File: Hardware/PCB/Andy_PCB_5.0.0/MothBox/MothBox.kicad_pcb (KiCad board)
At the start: 2 copper layers, 237.2 x 140.5 mm, 189 parts, among them J1 Screw_Terminal_01x02, J2 TYPE-C-31-M-17, J4 GPS Header, J5 Conn_01x05_Pin, J7 DC Power Jack, Q1 IRF9540N, Q10 BC817, Q11 BC817, Q2 TJ10S04M3L,LXHQ, Q3 BC817, Q4 TJ10S04M3L,LXHQ, Q5 TJ10S04M3L,LXHQ, Q6 BC817, Q7 BC817, Q8 BC817, Q9 BC817, SW1 SW_Push, SW2 Days, SW3 Power, SW4 Sequence+Toggle, SW5 Hours, SW6 Hours, U1 XL4015, U10 IRF9335TRPBF, U11 IRF9335TRPBF, U12 CD74HC4067M96E4, U13 CD74HC4067M96E4, U2 9V-36V to 12V 5A 60W, U3 RASPBERRY_PI_5, U4 RASPBERRY_PI_4B_4GB, U5 STM32L031K6Tx, U6 TLV75733PDBVR, U8 IRF9335TRPBF, U9 IRF9335TRPBF, Y1 32.768kHz

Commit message: made better camera
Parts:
- REF**: moved to F.Cu
- moved REF** 7.28 mm to (149.5, 131.8)
- moved REF** 3.00 mm to (125.5, 195.8)
- moved REF** 2.00 mm to (154.5, 195.8)
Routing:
- net Net-(Q5-G): track 8.96 -> 0.00 mm
- net /Photo LED's/+12V_R_LED: track 467.2 -> 476.2 mm
- net Net-(Q4-G): track 8.19 -> 0.00 mm
- net /Photo LED's/+12V_L_LED: track 483.1 -> 491.3 mm
- net Net-(Q2-G): track 7.03 -> 0.00 mm
- net /Power/VBUS: track 0.00 -> 7.03 mm
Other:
- outline, holes or cut-outs redrawn

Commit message: before overhaul from Troublemaker meeting
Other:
- board text added: "V5.0.0"

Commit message: added female inverted header
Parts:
- removed C10, C11: 12pF, Capacitor_SMD:C_0805_2012Metric
- removed C13, C14, C15, C18, C9: 0.1uF, Capacitor_SMD:C_0805_2012Metric
- removed C6, C7: 1uF, Capacitor_SMD:C_0805_2012Metric
- removed C8: 100nF, Capacitor_SMD:C_0805_2012Metric
- removed D10, D11, D12, D13, D14, D15, D16, D17, D18, D19, D2, D20, D3, D4, D5, D6, D7, D8, D9: LED, LED_SMD:LED_Everlight-SMD3528_3.5x2.8mm_67-21ST
- removed D21, D22, D23, D24, D25, D26, D27, D28: LED, LED_SMD:LED_0805_2012Metric
- removed D29, D36: ESD12VD3B-TP, Diode_SMD:D_SOD-323
- removed E1: BZT52Bxx, Diode_SMD:D_SOD-123F
- removed E2: SMBJ36A, Diode_SMD:D_SMB
- removed E4: SK54C, SK54C:DIO_SK54C
- removed F1: 7A Fuse, Fuse:Fuseholder_Clip-5x20mm_Eaton_1A5601-01_Inline_P20.80x6.76mm_D1.70mm_Horizontal
- removed J1: Screw_Terminal_01x02, TerminalBlock_RND:TerminalBlock_RND_205-00023_1x02_P10.00mm_Horizontal
- removed J2: TYPE-C-31-M-17, TYPE-C-31-M-17:TYPEC31M17
- removed J4: GPS Header, GPS_MAX10:Untitled
- removed J5: Conn_01x05_Pin, Connector_PinHeader_2.54mm:PinHeader_1x05_P2.54mm_Vertical
- removed J7: DC Power Jack, Connector_BarrelJack:BarrelJack_GCT_DCJ200-10-A_Horizontal
- removed Q1: IRF9540N, Package_TO_SOT_THT:TO-220-3_Vertical
- removed Q2: TJ10S04M3L,LXHQ, Package_TO_SOT_SMD:TO-252-2
- removed Q3: BC817, Package_TO_SOT_SMD:SOT-23
- removed R1: 10k, Resistor_SMD:R_0805_2012Metric
- removed R61, R62, R63, R64, R65, R67, R68, R70, R71, R72, R73, R74: 170R, Resistor_SMD:R_2512_6332Metric
- removed R83, R84, R85, R86: DNP, Resistor_SMD:R_0805_2012Metric
- removed REF** (x10): MountingHole_6.4mm_M6_Pad_wSTEP, AQLibrary:MountingHole_6.4mm_M6_Pad_wSTEP
- removed REF**: Arducam Owlsight, Attractor:Arducam Owlsight
- removed SW1: SW_Push, TS-1187A-B-A-B:SW_TS-1187A-B-A-B
- removed SW2: Days, DS04-254-2-07BK-SMT:SW_DS04-254-2-07BK-SMT
- removed SW3: Power, DS04-254-2-03BK-SMT1:SW_DS04-254-2-03BK-SMT
- removed SW4: Sequence+Toggle, DS04-254-2-04BK-SMT:SW_DS04-254-2-04BK-SMT
- removed SW5: Hours, DS04-254-2-07BK-SMT:SW_DS04-254-2-07BK-SMT
- removed SW6: Hours, DS04-254-2-06BK-SMT:SW_DS04-254-2-06BK-SMT
- removed Y1: 32.768kHz, Crystal:Crystal_SMD_3215-2Pin_3.2x1.5mm
- added B1: ~, AQLibrary:Talentcell, B.Cu at (117.2, 172.8)
- added D32: ESD12VD3B-TP, Diode_SMD:D_SOD-323, F.Cu at (22.1, 26.1)
- added F2: Polyfuse, Fuse:Fuse_Bourns_MF-RG1000, F.Cu at (203.7, 287.4)
- added H1: MountingHole_1/4inbolt, MountingHole:MountingHole_6.4mm_M6_Pad, F.Cu at (43.5, 70.8)
- added H2: MountingHole_1/4inbolt, MountingHole:MountingHole_6.4mm_M6_Pad, F.Cu at (155.5, 70.8)
- added H3: MountingHole_1/4inbolt, MountingHole:MountingHole_6.4mm_M6_Pad, F.Cu at (38.5, 77.8)
- added H4: MountingHole_1/4inbolt, MountingHole:MountingHole_6.4mm_M6_Pad, F.Cu at (163.5, 53.8)
- added H5: MountingHole_1/4inbolt, MountingHole:MountingHole_6.4mm_M6_Pad, F.Cu at (255.5, 192.8)
- added H6: MountingHole_1/4inbolt, MountingHole:MountingHole_6.4mm_M6_Pad, F.Cu at (41.5, 187.8)
- added H7: MountingHole_1/4inbolt, MountingHole:MountingHole_6.4mm_M6_Pad, F.Cu at (257.5, 178.8)
- added H8: MountingHole_1/4inbolt, MountingHole:MountingHole_6.4mm_M6_Pad, F.Cu at (42.5, 138.8)
- added LED1: XL-2835UWC-02, easyeda2kicad:LED-SMD_L3.5-W2.8-RD_1.25T-2PWT, F.Cu at (87.5, 223.8)
- added LED10: XL-2835UWC-02, easyeda2kicad:LED-SMD_L3.5-W2.8-RD_1.25T-2PWT, F.Cu at (94.1, 228.5)
- added LED11: XL-2835UWC-02, easyeda2kicad:LED-SMD_L3.5-W2.8-RD_1.25T-2PWT, F.Cu at (94.1, 232.5)
- added LED12: XL-2835UWC-02, easyeda2kicad:LED-SMD_L3.5-W2.8-RD_1.25T-2PWT, F.Cu at (94.1, 236.6)
- added LED13: XL-2835UWC-02, easyeda2kicad:LED-SMD_L3.5-W2.8-RD_1.25T-2PWT, F.Cu at (94.1, 240.6)
- added LED14: XL-2835UWC-02, easyeda2kicad:LED-SMD_L3.5-W2.8-RD_1.25T-2PWT, F.Cu at (94.1, 244.7)
- added LED15: XL-2835UWC-02, easyeda2kicad:LED-SMD_L3.5-W2.8-RD_1.25T-2PWT, F.Cu at (94.1, 248.7)
- added LED16: XL-2835UWC-02, easyeda2kicad:LED-SMD_L3.5-W2.8-RD_1.25T-2PWT, F.Cu at (94.1, 252.8)
- added LED17: XL-2835UWC-02, easyeda2kicad:LED-SMD_L3.5-W2.8-RD_1.25T-2PWT, F.Cu at (99.7, 224.4)
- added LED18: XL-2835UWC-02, easyeda2kicad:LED-SMD_L3.5-W2.8-RD_1.25T-2PWT, F.Cu at (99.7, 228.5)
- added LED19: XL-2835UWC-02, easyeda2kicad:LED-SMD_L3.5-W2.8-RD_1.25T-2PWT, F.Cu at (99.7, 232.5)
- added LED2: XL-2835UWC-02, easyeda2kicad:LED-SMD_L3.5-W2.8-RD_1.25T-2PWT, F.Cu at (88.5, 228.5)
- added LED20: XL-2835UWC-02, easyeda2kicad:LED-SMD_L3.5-W2.8-RD_1.25T-2PWT, F.Cu at (99.7, 236.6)
- added LED21: XL-2835UWC-02, easyeda2kicad:LED-SMD_L3.5-W2.8-RD_1.25T-2PWT, F.Cu at (99.7, 240.6)
- added LED22: XL-2835UWC-02, easyeda2kicad:LED-SMD_L3.5-W2.8-RD_1.25T-2PWT, F.Cu at (99.7, 244.7)
- added LED23: XL-2835UWC-02, easyeda2kicad:LED-SMD_L3.5-W2.8-RD_1.25T-2PWT, F.Cu at (99.7, 248.7)
- added LED24: XL-2835UWC-02, easyeda2kicad:LED-SMD_L3.5-W2.8-RD_1.25T-2PWT, F.Cu at (99.7, 252.8)
- added LED25: XL-2835UWC-02, easyeda2kicad:LED-SMD_L3.5-W2.8-RD_1.25T-2PWT, F.Cu at (105.3, 224.4)
- added LED26: XL-2835UWC-02, easyeda2kicad:LED-SMD_L3.5-W2.8-RD_1.25T-2PWT, F.Cu at (105.3, 228.5)
- added LED27: XL-2835UWC-02, easyeda2kicad:LED-SMD_L3.5-W2.8-RD_1.25T-2PWT, F.Cu at (105.3, 232.5)
- added LED28: XL-2835UWC-02, easyeda2kicad:LED-SMD_L3.5-W2.8-RD_1.25T-2PWT, F.Cu at (105.3, 236.6)
- added LED29: XL-2835UWC-02, easyeda2kicad:LED-SMD_L3.5-W2.8-RD_1.25T-2PWT, F.Cu at (105.3, 240.6)
- added LED3: XL-2835UWC-02, easyeda2kicad:LED-SMD_L3.5-W2.8-RD_1.25T-2PWT, F.Cu at (88.5, 232.5)
- added LED34: XL-2835UWC-02, easyeda2kicad:LED-SMD_L3.5-W2.8-RD_1.25T-2PWT, F.Cu at (105.3, 244.7)
- added LED35: XL-2835UWC-02, easyeda2kicad:LED-SMD_L3.5-W2.8-RD_1.25T-2PWT, F.Cu at (105.3, 248.7)
- added LED36: XL-2835UWC-02, easyeda2kicad:LED-SMD_L3.5-W2.8-RD_1.25T-2PWT, F.Cu at (105.3, 252.8)
- added LED37: XL-2835UWC-02, easyeda2kicad:LED-SMD_L3.5-W2.8-RD_1.25T-2PWT, F.Cu at (110.9, 224.4)
- added LED38: XL-2835UWC-02, easyeda2kicad:LED-SMD_L3.5-W2.8-RD_1.25T-2PWT, F.Cu at (110.9, 228.5)
- added LED39: XL-2835UWC-02, easyeda2kicad:LED-SMD_L3.5-W2.8-RD_1.25T-2PWT, F.Cu at (110.9, 232.5)
- added LED4: XL-2835UWC-02, easyeda2kicad:LED-SMD_L3.5-W2.8-RD_1.25T-2PWT, F.Cu at (88.5, 236.6)
- added LED40: XL-2835UWC-02, easyeda2kicad:LED-SMD_L3.5-W2.8-RD_1.25T-2PWT, F.Cu at (110.9, 236.6)
- added LED41: XL-2835UWC-02, easyeda2kicad:LED-SMD_L3.5-W2.8-RD_1.25T-2PWT, F.Cu at (110.9, 240.6)
- added LED42: XL-2835UWC-02, easyeda2kicad:LED-SMD_L3.5-W2.8-RD_1.25T-2PWT, F.Cu at (110.9, 244.7)
- added LED43: XL-2835UWC-02, easyeda2kicad:LED-SMD_L3.5-W2.8-RD_1.25T-2PWT, F.Cu at (110.9, 248.7)
- added LED44: XL-2835UWC-02, easyeda2kicad:LED-SMD_L3.5-W2.8-RD_1.25T-2PWT, F.Cu at (110.9, 252.8)
- added LED45: XL-2835UWC-02, easyeda2kicad:LED-SMD_L3.5-W2.8-RD_1.25T-2PWT, F.Cu at (116.5, 224.4)
- added LED46: XL-2835UWC-02, easyeda2kicad:LED-SMD_L3.5-W2.8-RD_1.25T-2PWT, F.Cu at (116.5, 228.5)
- added LED47: XL-2835UWC-02, easyeda2kicad:LED-SMD_L3.5-W2.8-RD_1.25T-2PWT, F.Cu at (116.5, 232.5)
- added LED48: XL-2835UWC-02, easyeda2kicad:LED-SMD_L3.5-W2.8-RD_1.25T-2PWT, F.Cu at (116.5, 236.6)
- added LED49: XL-2835UWC-02, easyeda2kicad:LED-SMD_L3.5-W2.8-RD_1.25T-2PWT, F.Cu at (116.5, 240.6)
- added LED5: XL-2835UWC-02, easyeda2kicad:LED-SMD_L3.5-W2.8-RD_1.25T-2PWT, F.Cu at (88.5, 240.6)
- added LED50: XL-2835UWC-02, easyeda2kicad:LED-SMD_L3.5-W2.8-RD_1.25T-2PWT, F.Cu at (116.5, 244.7)
- added LED51: XL-2835UWC-02, easyeda2kicad:LED-SMD_L3.5-W2.8-RD_1.25T-2PWT, F.Cu at (116.5, 248.7)
- added LED52: XL-2835UWC-02, easyeda2kicad:LED-SMD_L3.5-W2.8-RD_1.25T-2PWT, F.Cu at (116.5, 252.8)
- added LED6: XL-2835UWC-02, easyeda2kicad:LED-SMD_L3.5-W2.8-RD_1.25T-2PWT, F.Cu at (88.5, 244.7)
- added LED7: XL-2835UWC-02, easyeda2kicad:LED-SMD_L3.5-W2.8-RD_1.25T-2PWT, F.Cu at (88.5, 248.7)
- added LED8: XL-2835UWC-02, easyeda2kicad:LED-SMD_L3.5-W2.8-RD_1.25T-2PWT, F.Cu at (88.5, 252.8)
- added LED9: XL-2835UWC-02, easyeda2kicad:LED-SMD_L3.5-W2.8-RD_1.25T-2PWT, F.Cu at (94.1, 224.4)
- added P1: Raw Input, easyeda2kicad:CONN-TH_2P-P5.00_WJ500V-5.08-2P, F.Cu at (191.5, 291.9)
- added P2: 12V Regulated Input, easyeda2kicad:CONN-TH_2P-P5.00_WJ500V-5.08-2P, F.Cu at (191.5, 303.4)
- added P3: Input to regulator, easyeda2kicad:CONN-TH_2P-P5.00_WJ500V-5.08-2P, F.Cu at (191.5, 314.8)
- added P4: External Attractor, easyeda2kicad:CONN-TH_2P-P5.00_WJ500V-5.08-2P, F.Cu at (223.6, 291.9)
- added R43: DNP, Resistor_SMD:R_0805_2012Metric, F.Cu at (22.2, 12.3)
- added R44: DNP, Resistor_SMD:R_0805_2012Metric, F.Cu at (22.2, 15.2)
- added R45: 10k, Resistor_SMD:R_0805_2012Metric, F.Cu at (22.2, 18.2)
- added R46: 10k, Resistor_SMD:R_0805_2012Metric, F.Cu at (22.2, 21.1)
- added U14: ~, Attractor:Arducam Owlsight, F.Cu at (149.5, 131.8)
- added U16: Female Inv Socket Pi 2.54-2*20, easyeda2kicad:HDR-TH_40P-P2.54-V-F-R2-C20-S2.54, F.Cu at (236.5, 58.8)
- added U7: Modes, easyeda2kicad:SW-TH_16P-L21.7-W9.7-P2.54-BL, F.Cu at (31.7, 5.08)
- C17: value 1uF -> 0.1uF
- D1: value LED -> S10MC; footprint LED_SMD:LED_Everlight-SMD3528_3.5x2.8mm_67-21ST -> easyeda2kicad:SMC_L7.1-W6.2-LS8.1-RD
- D33: value IN-PI33TBTPRPGPB -> ESD12VD3B-TP; footprint IN-PI33TBTPRPGPB:LED_IN-PI33TBTPRPGPB -> Diode_SMD:D_SOD-323
- E3: value ESD5V0D3B -> SK54C; footprint Diode_SMD:D_SOD-323 -> SK54C:DIO_SK54C
- Q4: value TJ10S04M3L,LXHQ -> BC817; footprint Package_TO_SOT_SMD:TO-252-2 -> Package_TO_SOT_SMD:SOT-23
- Q7: value BC817 -> TJ10S04M3L,LXHQ; footprint Package_TO_SOT_SMD:SOT-23 -> Package_TO_SOT_SMD:TO-252-2
- R10, R12, R13, R14, R15, R2, R53, R7, R8, R9: value 1k -> FRC0805F30R0TS; footprint Resistor_SMD:R_0805_2012Metric -> easyeda2kicad:R0805
- R11, R6: value 10K -> FRC0805F30R0TS; footprint Resistor_SMD:R_0805_2012Metric -> easyeda2kicad:R0805
- R21, R23, R25, R26, R39, R42: value 10k -> DNP
- R3, R51, R52: value 10k -> FRC0805F30R0TS; footprint Resistor_SMD:R_0805_2012Metric -> easyeda2kicad:R0805
- R47, R48, R49, R50: value DNP -> 10k
- R55: value 170R -> FRC0805F30R0TS; footprint Resistor_SMD:R_2512_6332Metric -> easyeda2kicad:R0805
- R56, R57, R58, R59, R60, R69: value 170R -> 10k; footprint Resistor_SMD:R_2512_6332Metric -> Resistor_SMD:R_0805_2012Metric
- R66: value 170R -> 1k; footprint Resistor_SMD:R_2512_6332Metric -> Resistor_SMD:R_0805_2012Metric
- R79: value 10k -> 1k
- R81: value 1k -> 10k
- U1: value XL4015 -> days; footprint XL4015:CONV_XL4015 -> easyeda2kicad:SW-TH_16P-L21.7-W9.7-P2.54-BL
- U12, U13: value CD74HC4067M96E4 -> IRF9335TRPBF; footprint CD74HC4067M96E4:SOIC127P1030X265-24N -> Package_SO:SOIC-8_3.9x4.9mm_P1.27mm
- U2: value 9V-36V to 12V 5A 60W -> hours1; footprint TerminalBlock:TerminalBlock_MaiXu_MX126-5.0-04P_1x04_P5.00mm -> easyeda2kicad:SW-TH_16P-L21.7-W9.7-P2.54-BL
- U3: value RASPBERRY_PI_5 -> XL4015E1; footprint Connector_PinHeader_2.54mm:PinHeader_2x20_P2.54mm_Vertical -> easyeda2kicad:TO-263-5_L10.2-W8.9-P1.70-TL
- U5: value STM32L031K6Tx -> RASPBERRY_PI_5; footprint Package_QFP:LQFP-32_7x7mm_P0.8mm -> Connector_PinHeader_2.54mm:PinHeader_2x20_P2.54mm_Vertical
- U6: value TLV75733PDBVR -> hours2; footprint TLV75733PDBVR:SOT95P280X145-5N -> easyeda2kicad:SW-TH_16P-L21.7-W9.7-P2.54-BL
- U8, U9: value IRF9335TRPBF -> CD74HC4067M96E4; footprint Package_SO:SOIC-8_3.9x4.9mm_P1.27mm -> CD74HC4067M96E4:SOIC127P1030X265-24N
- moved U9 262.9 mm to (358.5, 145.8)
- moved D1 261.8 mm to (202.7, 294.0), turned to 0 degrees
- moved U6 204.6 mm to (328.5, 178.8), turned to -90 degrees
- moved U5 182.3 mm to (254.6, 67.5), turned to -90 degrees
- moved E3 181.3 mm to (389.5, 125.8)
- moved Q10 166.8 mm to (389.0, 92.8)
- moved R79 166.8 mm to (385.5, 92.7)
- moved R81 166.8 mm to (392.5, 92.8)
- moved U10 166.8 mm to (380.1, 91.2)
- moved U8 153.0 mm to (327.5, 73.8), turned to 0 degrees
- moved R11 137.0 mm to (-4.50, 258.8)
- moved R6 137.0 mm to (9.72, 245.5)
- moved U1 130.6 mm to (351.5, 75.8), turned to 90 degrees
- moved R8 130.1 mm to (9.50, 259.8)
- moved R10 126.0 mm to (35.4, 259.8)
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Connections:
- C3 pad 2: Net-(U1-VC) -> Net-(U3-VC)
- D1 pad 1: GND -> +12V
- D30 pad 1: /UV LED PCB/+12V_PCB3 -> /UV LED PCB/+12V_PCB1
- D33 pad 1: GND -> /UV LED PCB/+12V_PCB4
- D33 pad 2: /RPI5+MCU/PA12 -> GND
- L1 pad 1: Net-(E4-PadC) -> Net-(E3-PadC)
- Q4 pad 1: /Photo LED's/+12V_L_LED -> Net-(Q4-B)
- Q4 pad 2: Net-(Q4-G) -> GND
- Q4 pad 3: +12V -> Net-(Q4-C)
- Q5 pad 1: /Photo LED's/+12V_R_LED -> /Photo LED's/+12V_L_LED
- Q5 pad 2: Net-(Q5-G) -> Net-(Q4-C)
- Q6 pad 3: Net-(Q4-G) -> Net-(Q6-C)
- Q7 pad 1: Net-(Q7-B) -> /Photo LED's/+12V_R_LED
- Q7 pad 2: GND -> Net-(Q6-C)
- Q7 pad 3: Net-(Q5-G) -> +12V
- R10 pad 1: /RPI5+MCU/PA3 -> Net-(LED20-A)
- R10 pad 2: Net-(D24-A) -> /Photo LED's/+12V_R_LED
- R11 pad 1: /RPI5+MCU/BOOT0 -> Net-(LED23-A)
- R11 pad 2: GND -> /Photo LED's/+12V_R_LED
- R12 pad 1: /RPI5+MCU/PA4 -> Net-(LED26-A)
- R12 pad 2: Net-(D25-A) -> /Photo LED's/+12V_R_LED
- R13 pad 1: /RPI5+MCU/PA5 -> Net-(LED29-A)
- R13 pad 2: Net-(D26-A) -> /Photo LED's/+12V_R_LED
- R14 pad 1: /RPI5+MCU/PA6 -> Net-(LED38-A)
- R14 pad 2: Net-(D27-A) -> /Photo LED's/+12V_R_LED
- R15 pad 1: /RPI5+MCU/PA7 -> Net-(LED41-A)
- R15 pad 2: Net-(D28-A) -> /Photo LED's/+12V_R_LED
- R16 pad 2: /GPS+Switches/Tue -> /Switches/Mon
- R17 pad 2: /GPS+Switches/Thur -> /Switches/Tue
- R18 pad 2: /GPS+Switches/Sat -> /Switches/Wed
- R19 pad 2: /GPS+Switches/Med_PW -> /Switches/Thur
- R2 pad 2: RPI_CTRL -> /Photo LED's/+12V_L_LED
- R20 pad 2: /GPS+Switches/Seq_2 -> /Switches/Fri
- R21 pad 2: /GPS+Switches/Armed/Disarmed -> S0_MUX
- R22 pad 2: /GPS+Switches/Hour_2 -> /Switches/Sat
- R23 pad 2: /GPS+Switches/Hour_4 -> S1_MUX
- R24 pad 2: /GPS+Switches/Hour_6 -> /Switches/Sun
- R25 pad 2: /GPS+Switches/Hour_9 -> S2_MUX
- R26 pad 2: /GPS+Switches/Hour_11 -> S3_MUX
- R27 pad 2: /GPS+Switches/Hour_13 -> /Switches/Attractor_3
- R28 pad 2: /GPS+Switches/Mon -> /Switches/Attractor_2
- R29 pad 2: /GPS+Switches/Wed -> /Switches/Attractor_1
- R3 pad 1: GND -> Net-(LED6-A)
- R3 pad 2: Net-(E1-A) -> /Photo LED's/+12V_L_LED
- R30 pad 2: /GPS+Switches/Fri -> /Switches/C1
- R31 pad 2: /GPS+Switches/Sun -> /Switches/INT/EXT_Attractor
- R32 pad 2: /GPS+Switches/Min_PW -> /Switches/HI/LOW_PWR
- R33 pad 2: /GPS+Switches/Max_PW -> /Switches/Test_Debug
- R34 pad 2: /GPS+Switches/Seq_1 -> /Switches/Hour_1
- R35 pad 2: /GPS+Switches/Seq_3 -> /Switches/Hour_2
- R36 pad 2: /GPS+Switches/Hour_1 -> /Switches/Hour_3
- R37 pad 2: /GPS+Switches/Hour_3 -> /Switches/Hour_4
- R38 pad 2: /GPS+Switches/Hour_5 -> /Switches/Hour_5
- R39 pad 1: +3.3V -> S3_MUX
- R39 pad 2: /GPS+Switches/Hour_7 -> GND
- R40 pad 2: /GPS+Switches/Hour_8 -> /Switches/Hour_6
- R41 pad 2: /GPS+Switches/Hour_10 -> /Switches/Hour_7
- R42 pad 1: +3.3V -> S2_MUX
- R42 pad 2: /GPS+Switches/Hour_12 -> GND
- R47 pad 1: S3_MUX -> +3.3V
- R47 pad 2: GND -> /Switches/Hour_11
- R48 pad 1: S2_MUX -> +3.3V
- R48 pad 2: GND -> /Switches/Hour_12
- R49 pad 1: S1_MUX -> +3.3V
- R49 pad 2: GND -> /Switches/Hour_13
- R50 pad 1: S0_MUX -> +3.3V
- R50 pad 2: GND -> /Switches/Hour_14
- R51 pad 1: Net-(Q4-G) -> Net-(LED12-A)
- R51 pad 2: +12V -> /Photo LED's/+12V_L_LED
- R52 pad 1: Net-(Q5-G) -> Net-(LED44-A)
- R52 pad 2: +12V -> /Photo LED's/+12V_R_LED
- R53 pad 1: Net-(Q6-B) -> Net-(LED47-A)
- R53 pad 2: L_LED_CTRL -> /Photo LED's/+12V_L_LED
- R54 pad 1: Net-(Q7-B) -> Net-(Q4-B)
- R55 pad 1: /Photo LED's/+12V_L_LED -> Net-(LED50-A)
- R55 pad 2: Net-(D1-A) -> /Photo LED's/+12V_R_LED
- R56 pad 1: /Photo LED's/+12V_L_LED -> +3.3V
- R56 pad 2: Net-(D2-A) -> /Switches/Hour_8
- R57 pad 1: /Photo LED's/+12V_L_LED -> Net-(Q4-C)
- R57 pad 2: Net-(D3-A) -> +12V
- R58 pad 1: /Photo LED's/+12V_L_LED -> +3.3V
- R58 pad 2: Net-(D4-A) -> /Switches/Hour_15
- R59 pad 1: /Photo LED's/+12V_L_LED -> +3.3V
- R59 pad 2: Net-(D5-A) -> /Switches/Hour_16
- R6 pad 1: +3.3V -> Net-(LED9-A)
- R6 pad 2: /RPI5+MCU/NRST -> /Photo LED's/+12V_L_LED
- R60 pad 1: /Photo LED's/+12V_L_LED -> +3.3V
- R60 pad 2: Net-(D6-A) -> /Switches/C2
- R66 pad 1: /Photo LED's/+12V_R_LED -> Net-(Q6-B)
- R66 pad 2: Net-(D12-A) -> L_LED_CTRL
- R69 pad 1: /Photo LED's/+12V_R_LED -> Net-(Q6-C)
- R69 pad 2: Net-(D15-A) -> +12V
- R7 pad 1: /RPI5+MCU/PA8 -> Net-(LED13-A)
- R7 pad 2: Net-(D21-A) -> /Photo LED's/+12V_L_LED
- R79 pad 1: Net-(Q10-C) -> Net-(Q10-B)
- R79 pad 2: +12V -> UV1_CTRL
- R8 pad 1: /RPI5+MCU/PA11 -> Net-(LED16-A)
- R8 pad 2: Net-(D22-A) -> /Photo LED's/+12V_L_LED
- R80 pad 2: UV1_CTRL -> UV4_EX_CTRL
- R81 pad 1: Net-(Q10-B) -> Net-(Q10-C)
- R81 pad 2: UV4_EX_CTRL -> +12V
- R9 pad 1: /RPI5+MCU/PA2 -> Net-(LED19-A)
- R9 pad 2: Net-(D23-A) -> /Photo LED's/+12V_L_LED
- U1 pad 2: /Power/FB -> GND
- U1 pad 3: Net-(E4-PadC) -> GND
- U1 pad 4: Net-(U1-VC) -> GND
- U1 pad 5: /Power/PWR_IN -> GND
- U10 pad 4: Net-(Q10-C) -> Net-(Q8-C)
- U10 pad 5: /UV LED PCB/+12V_PCB4 -> /UV LED PCB/+12V_PCB1
- U10 pad 6: /UV LED PCB/+12V_PCB4 -> /UV LED PCB/+12V_PCB1
- U10 pad 7: /UV LED PCB/+12V_PCB4 -> /UV LED PCB/+12V_PCB1
- U10 pad 8: /UV LED PCB/+12V_PCB4 -> /UV LED PCB/+12V_PCB1
- U11 pad 4: Net-(Q11-C) -> Net-(Q9-C)
- U12 pad 1: COM_I/O -> +12V
- U12 pad 2: unconnected-(U12-I7-Pad2) -> +12V
- U12 pad 3: /GPS+Switches/Thur -> +12V
- U12 pad 4: /GPS+Switches/Fri -> Net-(Q10-C)
- U12 pad 5: /GPS+Switches/Sat -> /UV LED PCB/+12V_PCB3
- U12 pad 6: /GPS+Switches/Sun -> /UV LED PCB/+12V_PCB3
- U12 pad 7: /GPS+Switches/Mon -> /UV LED PCB/+12V_PCB3
- U12 pad 8: /GPS+Switches/Tue -> /UV LED PCB/+12V_PCB3
- U13 pad 1: COM_I/O -> +12V
- U13 pad 2: unconnected-(U13-I7-Pad2) -> +12V
- U13 pad 3: /GPS+Switches/Hour_7 -> +12V
- U13 pad 4: /GPS+Switches/Hour_6 -> Net-(Q11-C)
- U13 pad 5: /GPS+Switches/Hour_5 -> /UV LED PCB/+12V_PCB4
- U13 pad 6: /GPS+Switches/Hour_4 -> /UV LED PCB/+12V_PCB4
- U13 pad 7: /GPS+Switches/Hour_3 -> /UV LED PCB/+12V_PCB4
- U13 pad 8: /GPS+Switches/Hour_2 -> /UV LED PCB/+12V_PCB4
- U2 pad 1: /Power/PWR_IN -> GND
- U2 pad 4: +12V -> GND
- U3 pad 1: +3.3V -> GND
- U3 pad 2: Net-(RJ1-Pad2) -> /Power/FB
- U3 pad 3: GPS_SDA -> Net-(E3-PadC)
- U3 pad 4: Net-(RJ1-Pad2) -> Net-(U3-VC)
- U3 pad 5: GPS_SCL -> /Power/PWR_IN
- U3 pad 6: GND -> unconnected-(U3-SW-Pad6)
- U5 pad 10: /RPI5+MCU/PA4 -> /RPI5/STM_RX
- U5 pad 11: /RPI5+MCU/PA5 -> /RPI5/Save for eink_11
- U5 pad 12: /RPI5+MCU/PA6 -> S2_MUX
- U5 pad 13: /RPI5+MCU/PA7 -> S1_MUX
- U5 pad 14: unconnected-(U5-PB0-Pad14) -> GND
- U5 pad 15: unconnected-(U5-PB1-Pad15) -> S3_MUX
- U5 pad 16: GND -> EN_MUX1
- U5 pad 18: /RPI5+MCU/PA8 -> /RPI5/Save for eink_18
- U5 pad 19: /RPI5+MCU/STM_RX -> /RPI5/Save for eink_19
- U5 pad 2: /RPI5+MCU/OSC_IN -> Net-(RJ1-Pad2)
- U5 pad 20: /RPI5+MCU/STM_TX -> GND
- U5 pad 21: /RPI5+MCU/PA11 -> UV1_CTRL
- U5 pad 22: /RPI5+MCU/PA12 -> /RPI5/Save for eink_22
- U5 pad 23: /RPI5+MCU/SWDIO -> /RPI5/Save for eink_23
- U5 pad 24: /RPI5+MCU/SWDCLK -> /RPI5/Save for eink_24
- U5 pad 25: unconnected-(U5-PA15-Pad25) -> GND
- U5 pad 26: unconnected-(U5-PB3-Pad26) -> UV4_EX_CTRL
- U5 pad 27: unconnected-(U5-PB4-Pad27) -> /RPI5/ID_SD
- U5 pad 28: unconnected-(U5-PB5-Pad28) -> /RPI5/ID_SC
- U5 pad 29: unconnected-(U5-PB6-Pad29) -> EN_MUX2
- U5 pad 3: /RPI5+MCU/OSC_OUT -> GPS_SDA
- U5 pad 30: unconnected-(U5-PB7-Pad30) -> GND
- U5 pad 31: /RPI5+MCU/BOOT0 -> L_LED_CTRL
- U5 pad 32: GND -> /RPI5/TimeP
- U5 pad 4: /RPI5+MCU/NRST -> Net-(RJ1-Pad2)
- U5 pad 5: +3.3V -> GPS_SCL
- U5 pad 6: unconnected-(U5-PA0-Pad6) -> GND
- U5 pad 7: unconnected-(U5-PA1-Pad7) -> /RPI5/GPIO4/GPIO_GCKL
- U5 pad 8: /RPI5+MCU/PA2 -> /RPI5/STM_TX
- U5 pad 9: /RPI5+MCU/PA3 -> GND
- U6 pad 1: +5V -> GND
- U6 pad 3: +5V -> GND
- U6 pad 4: (no net) -> GND
- U6 pad 5: +3.3V -> GND
- U8 pad 1: +12V -> COM_I/O
- U8 pad 2: +12V -> /Switches/Test_Debug
- U8 pad 3: +12V -> /Switches/Thur
- U8 pad 4: Net-(Q8-C) -> /Switches/Fri
- U8 pad 5: /UV LED PCB/+12V_PCB1 -> /Switches/Sat
- U8 pad 6: /UV LED PCB/+12V_PCB1 -> /Switches/Sun
- U8 pad 7: /UV LED PCB/+12V_PCB1 -> /Switches/Mon
- U8 pad 8: /UV LED PCB/+12V_PCB1 -> /Switches/Tue
- U9 pad 1: +12V -> COM_I/O
- U9 pad 2: +12V -> /Switches/Hour_8
- U9 pad 3: +12V -> /Switches/Hour_7
- U9 pad 4: Net-(Q9-C) -> /Switches/Hour_6
- U9 pad 5: /UV LED PCB/+12V_PCB3 -> /Switches/Hour_5
- U9 pad 6: /UV LED PCB/+12V_PCB3 -> /Switches/Hour_4
- U9 pad 7: /UV LED PCB/+12V_PCB3 -> /Switches/Hour_3
- U9 pad 8: /UV LED PCB/+12V_PCB3 -> /Switches/Hour_2
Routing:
- net /Photo LED's/+12V_L_LED: track 491.3 -> 0.00 mm
- net /Photo LED's/+12V_R_LED: track 476.2 -> 0.00 mm
- net +3.3V: track 555.9 -> 292.2 mm, vias 6 -> 3
- net COM_I/O: track 239.5 -> 0.00 mm, vias 4 -> 0
- net S0_MUX: track 231.9 -> 0.00 mm, vias 4 -> 0
- net EN_MUX2: track 223.1 -> 0.00 mm, vias 3 -> 0
- net UV1_CTRL: track 213.9 -> 0.00 mm, vias 2 -> 0
- net S3_MUX: track 213.2 -> 0.00 mm, vias 3 -> 0
- net S2_MUX: track 210.3 -> 0.00 mm, vias 3 -> 0
- net S1_MUX: track 204.4 -> 0.00 mm, vias 1 -> 0
- net /RPI5+MCU/STM_TX: track 203.5 -> 0.00 mm, vias 3 -> 0
- net /RPI5+MCU/STM_RX: track 202.3 -> 0.00 mm, vias 3 -> 0
- net EN_MUX1: track 200.6 -> 0.00 mm, vias 2 -> 0
- net /RPI5+MCU/SWDCLK: track 200.2 -> 0.00 mm, vias 2 -> 0
- net /RPI5+MCU/SWDIO: track 197.6 -> 0.00 mm, vias 2 -> 0
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- added copper zone on B.Cu, net (none)
- added copper zone on F.Cu, net (none)
- added copper zone on F.Cu, net Net-(E3-PadC)
- removed copper zone on B.Cu, net /Power/VBUS
- removed copper zone on B.Cu, net Net-(E1-K)
- removed copper zone on F.Cu, net Net-(E2-K)
- removed copper zone on F.Cu, net Net-(E4-PadC)
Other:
- board text removed: "3.3V"
- board text removed: "GND"
- board text removed: "NRST"
- board text removed: "SWDCLK"
- board text removed: "SWDIO"

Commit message: made vertical pi
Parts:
- removed U4: RASPBERRY_PI_4B_4GB, RASPBERRY_PI_4B_4GB:MODULE_RASPBERRY_PI_4B_4GB
- added U18: RASPBERRY_PI_4B_4GB, RASPBERRY_PI_4B_4GB:MODULE_RASPBERRY_PI_4B_4GB_Sideways, B.Cu at (90.5, 82.8)
- U16: footprint easyeda2kicad:HDR-TH_40P-P2.54-V-F-R2-C20-S2.54 -> easyeda2kicad:HDR-TH_40P-P2.54-H-F-R2-C20-W8.5; moved to B.Cu
- U5: moved to B.Cu
- moved H3 217.1 mm to (255.5, 72.8)
- moved U16 160.7 mm to (80.5, 97.5), turned to 0 degrees
- moved U5 71.5 mm to (258.2, 138.9), turned to 0 degrees
- moved U3 16.0 mm to (302.5, 105.8)
- moved R49 9.96 mm to (74.7, 106.8)
- moved R50 9.96 mm to (72.5, 106.8)
- moved H1 5.00 mm to (39.5, 73.8)
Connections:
- U16 pad 39: /RPI5/Save for relay 3 -> /RPI5/Save for relay 2
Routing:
- net +3.3V: track 292.2 -> 245.1 mm
- net GND: track 37.2 -> 5.13 mm, vias 371 -> 357
- net +12V: track 64.8 -> 62.0 mm
- net Net-(Q9-C): track 2.69 -> 0.00 mm
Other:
- board size 237.2 x 140.5 mm -> 237 x 140.5 mm

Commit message: arranged stuff better
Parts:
- D1, L1, U7: moved to B.Cu
- F2: footprint Fuse:Fuse_Bourns_MF-RG1000 -> easyeda2kicad:F0805; moved to B.Cu
- P1, P2, P3, P4: footprint easyeda2kicad:CONN-TH_2P-P5.00_WJ500V-5.08-2P -> easyeda2kicad:CONN-TH_DB301V-3.5-2P-GN; moved to B.Cu
- U1: value days -> Days; moved to B.Cu
- U2: value hours1 -> Hours1
- U6: value hours2 -> Hours2; moved to B.Cu
- U8, U9: footprint CD74HC4067M96E4:SOIC127P1030X265-24N -> easyeda2kicad:SOIC-24_L15.4-W7.5-P1.27-LS10.3-BL
- moved U7 191.8 mm to (190.5, 112.8), turned to 180 degrees
- moved E3 178.2 mm to (211.5, 133.8)
- moved U6 161.3 mm to (190.3, 95.6), turned to 180 degrees
- moved P2 160.7 mm to (259.5, 157.8), turned to 90 degrees
- moved P3 160.2 mm to (259.5, 169.8), turned to 90 degrees
- moved D1 156.9 mm to (259.5, 147.8), turned to 180 degrees
- moved U1 142.8 mm to (213.5, 112.6), turned to 180 degrees
- moved P1 132.7 mm to (259.5, 177.9), turned to 90 degrees
- moved H7 130.3 mm to (380.5, 221.8)
- moved F2 129.3 mm to (265.5, 173.8), turned to -90 degrees
- moved U9 129.1 mm to (239.5, 95.8)
- moved U2 101.2 mm to (213.5, 95.6), turned to 180 degrees
- moved C4 98.1 mm to (183.5, 133.8), turned to 0 degrees
- moved P4 98.0 mm to (242.5, 195.8)
- moved U8 97.1 mm to (239.5, 114.8)
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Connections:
- F2 pad 1: Net-(F2-Pad1) -> /Power/PWR_IN
- F2 pad 2: /Power/PWR_IN -> Net-(F2-Pad2)
- P1 pad 2: Net-(F2-Pad1) -> Net-(F2-Pad2)
- U8 pad 15: EN_MUX1 -> GND
- U9 pad 15: EN_MUX2 -> GND
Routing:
- net +3.3V: track 245.1 -> 29.0 mm, vias 3 -> 0
- net +12V: track 62.0 -> 0.00 mm, vias 30 -> 0
- net +5V: track 14.7 -> 0.00 mm, vias 16 -> 0
- net GND: track 5.13 -> 2.53 mm, vias 357 -> 144
- net /Power/PWR_IN: vias 16 -> 0
- net (no net): vias 2 -> 0
- removed copper zone on B.Cu, net (none)
- removed copper zone on F.Cu, net +12V
- removed copper zone on B.Cu, net +5V
- removed copper zone on B.Cu, net /Power/PWR_IN
- removed copper zone on B.Cu, net /UV LED PCB/+12V_PCB1
- removed copper zone on B.Cu, net /UV LED PCB/+12V_PCB2
- removed copper zone on B.Cu, net /UV LED PCB/+12V_PCB3
- removed copper zone on B.Cu, net /UV LED PCB/+12V_PCB4
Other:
- board text added: "---------HOURS----------"
- board text added: "--------DAYS---------"
- board text added: "--------MODE---------"
- board text added: "01 02 03 04 05 06 07 08"
- board text added: "17 18 19 20 21 22 23 00"
- board text added: "ARM Mo Tu We Th Fr Sa Su"
- board text added: "C1 C2 A1 A2 A3 EXT HI DEBUG"
- board text added: "RAW INPUT"
- board text added: "Regulated 12V+"
- board text added: "to Regulator"
- board text removed: "00 01 02 03 04 05"
- board text removed: "06 07 c1 ARM"
- board text removed: "17 18 19 20 21 22 23"
- board text removed: "GPS"
- board text removed: "MO TU WE TH FR SA SU"

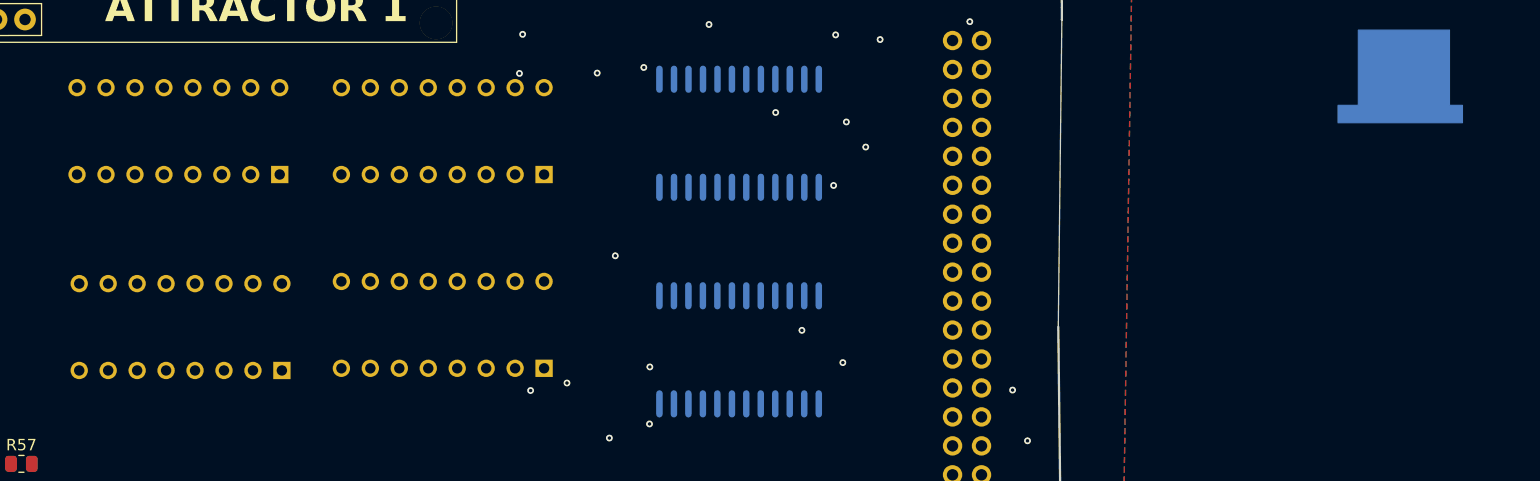
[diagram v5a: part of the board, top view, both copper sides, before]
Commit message: made regulator switch on and off and SMD switches
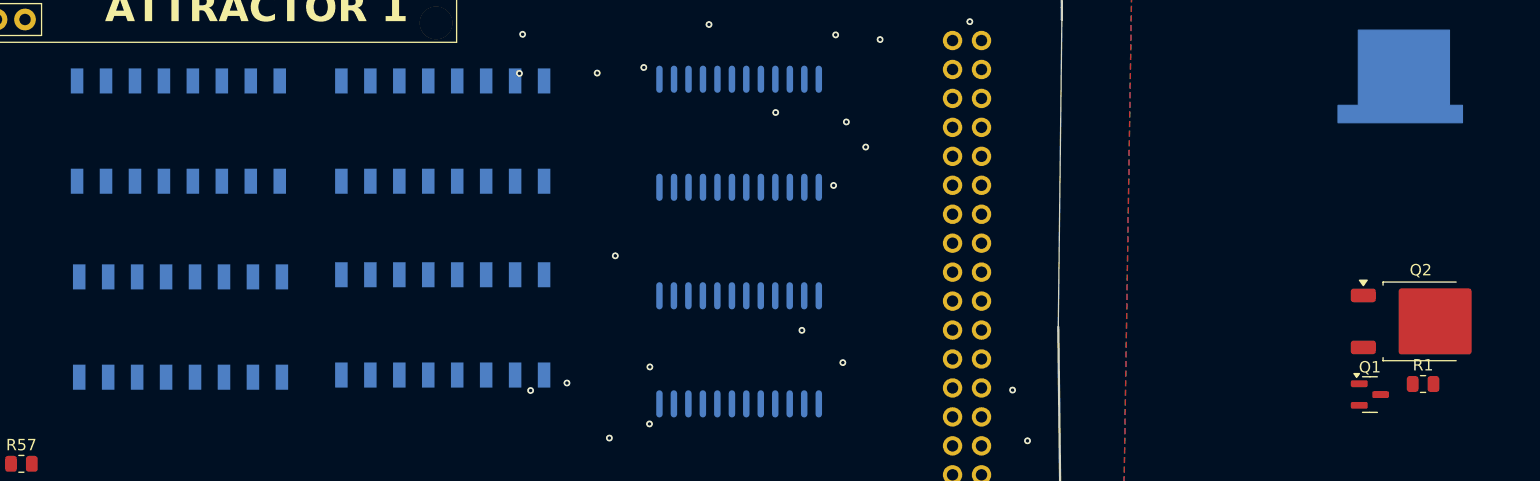
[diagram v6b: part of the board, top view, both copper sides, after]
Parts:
- added Q1: BC817, Package_TO_SOT_SMD:SOT-23, F.Cu at (294.8, 118.7)
- added Q2: TJ10S04M3L,LXHQ, Package_TO_SOT_SMD:TO-252-2, F.Cu at (299.3, 112.3)
- added R1: 10k, Resistor_SMD:R_0805_2012Metric, F.Cu at (299.5, 117.8)
- U1, U2, U6, U7: footprint easyeda2kicad:SW-TH_16P-L21.7-W9.7-P2.54-BL -> easyeda2kicad:SW-SMD_SMXS-08K-TP
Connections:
- U16 pad 15: EN_MUX1 -> EN_12VReg
- U5 pad 16: EN_MUX1 -> EN_12VReg

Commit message: Added adafruit current sensor
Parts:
- removed RJ1: 0R, Resistor_SMD:R_2512_6332Metric
- added C6: 0.1µF, easyeda2kicad:C0603, B.Cu at (231.5, 176.8)
- added R61: 10K, easyeda2kicad:R0603, B.Cu at (240.2, 171.6)
- added R62: 10K, easyeda2kicad:R0603, B.Cu at (240.2, 174.1)
- added R63: 0.1/1% (PT2512FK-070R1L), easyeda2kicad:R2512, B.Cu at (233.7, 172.9)
- added R64: 10K, easyeda2kicad:R0603, B.Cu at (240.2, 176.5)
- added R65: 10K, easyeda2kicad:R0603, B.Cu at (240.2, 179.0)
- added SJ1: SOLDERJUMPERREFLOW_NOPASTE, Jumper:SolderJumper-2_P1.3mm_Open_RoundedPad1.0x1.5mm, B.Cu at (233.5, 193.8)
- added SJ2: SOLDERJUMPERREFLOW_NOPASTE, Jumper:SolderJumper-2_P1.3mm_Open_TrianglePad1.0x1.5mm, B.Cu at (233.5, 196.8)
- added U19: INA219BIDCNT, easyeda2kicad:SOT-23-8_L3.0-W1.7-P0.65-LS2.8-BR, B.Cu at (235.9, 177.5)
- Q1, Q2, R1: moved to B.Cu
- moved R79 126.1 mm to (220.9, 151.3)
- moved Q10 126.1 mm to (224.4, 151.4)
- moved R81 126.1 mm to (227.9, 151.4)
- moved U10 126.1 mm to (215.5, 149.8)
- moved C5 111.7 mm to (221.9, 159.4)
- moved U3 80.9 mm to (245.5, 147.8)
- moved R1 63.1 mm to (238.6, 134.3), turned to 180 degrees
- moved Q2 62.7 mm to (238.8, 128.8), turned to 180 degrees
- moved Q1 54.1 mm to (243.3, 135.2), turned to 180 degrees
- moved U5 3.00 mm to (258.2, 138.9)
- moved D32 2.19 mm to (23.5, 27.8)
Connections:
- net GPS_SCL renamed SCL
- net GPS_SDA renamed SDA
- F2 pad 1: /Power/PWR_IN -> /Power/VIN+
- Q1 pad 1: unconnected-(Q1-B-Pad1) -> EN_12VReg
- U16 pad 1: Net-(RJ1-Pad2) -> +5V
- U16 pad 3: Net-(RJ1-Pad2) -> +5V
- U5 pad 2: Net-(RJ1-Pad2) -> +5V
- U5 pad 4: Net-(RJ1-Pad2) -> +5V
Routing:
- net GND: vias 144 -> 143
- removed copper zone on F.Cu, net (none)
- removed copper zone on F.Cu, net +5V
- removed copper zone on F.Cu, net /Power/PWR_IN
- removed copper zone on F.Cu, net Net-(E3-PadC)
